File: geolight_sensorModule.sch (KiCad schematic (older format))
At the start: 19 parts, among them IC1 ATTINY841-SSU, P1 5V, P2 ICSP, P3 IN, P4 OUT, P5 AUX_SENSOR, P6 UART, U1 TCRT5000/L, Y1 16Mhz

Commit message: re-arranged PCB, routing done (all except ground plane)
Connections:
- net RESET: now also IC1.4 ((PCINT11/dW/~RESET~/ADC9)PB3), R4.2
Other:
- moved on the sheet: R4
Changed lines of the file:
@@
 L +5V #PWR01
 U 1 1 57C9E241
-P 3050 2300
-F 0 "#PWR01" H 3050 2150 50  0001 C CNN
-F 1 "+5V" H 3050 2440 50  0000 C CNN
-F 2 "" H 3050 2300 50  0000 C CNN
-F 3 "" H 3050 2300 50  0000 C CNN
-	1    3050 2300
+P 2850 2300
+F 0 "#PWR01" H 2850 2150 50  0001 C CNN
+F 1 "+5V" H 2850 2440 50  0000 C CNN
+F 2 "" H 2850 2300 50  0000 C CNN
+F 3 "" H 2850 2300 50  0000 C CNN
+	1    2850 2300
 	1    0    0    -1
 $EndComp
@@
 U 1 1 57CBB75B
 P 2950 4400
-F 0 "Y1" V 3150 4450 60  0000 C CNN
+F 0 "Y1" V 3100 4600 60  0000 C CNN
 F 1 "16Mhz" V 2750 4450 60  0000 C CNN
 F 2 "Crystals:Resonator_3.2x1.3mm" H 2970 4360 60  0001 C CNN
@@
 L R_Small R4
 U 1 1 57CC33DC
-P 3050 3800
-F 0 "R4" H 2900 3950 50  0000 L CNN
-F 1 "10k" V 2950 3750 50  0000 L CNN
-F 2 "Resistors_SMD:R_0603" H 3050 3800 50  0001 C CNN
-F 3 "" H 3050 3800 50  0000 C CNN
-	1    3050 3800
+P 2850 3800
+F 0 "R4" H 2700 3950 50  0000 L CNN
+F 1 "10k" V 2750 3750 50  0000 L CNN
+F 2 "Resistors_SMD:R_0603" H 2850 3800 50  0001 C CNN
+F 3 "" H 2850 3800 50  0000 C CNN
+	1    2850 3800
 	1    0    0    -1
 $EndComp
@@
 	5200 2300 5200 2350
 Wire Wire Line
-	5550 2350 5900 2350
+	5550 2350 5700 2350
+Wire Wire Line
+	5700 2350 5900 2350
 Wire Wire Line
 	5250 3600 5450 3600
@@
 	4500 2300 4500 2400
 Wire Wire Line
-	4300 2400 4700 2400
+	4300 2400 4500 2400
+Wire Wire Line
+	4500 2400 4700 2400
 Connection ~ 4500 2800
 Wire Wire Line
 	4500 2900 4500 2800
 Wire Wire Line
-	4300 2800 4700 2800
+	4300 2800 4500 2800
+Wire Wire Line
+	4500 2800 4700 2800
 Wire Wire Line
 	4700 2400 4700 2500
 Wire Wire Line
 	4700 2800 4700 2700
-Connection ~ 3050 3400
-Wire Wire Line
-	3050 2300 3050 3700
-Wire Wire Line
-	3050 4200 3050 3900
-Wire Wire Line
-	3150 4200 3050 4200
+Connection ~ 2850 3400
+Wire Wire Line
+	2850 2300 2850 3400
+Wire Wire Line
+	2850 3400 2850 3700
+Wire Wire Line
+	2850 4200 2850 3900
+Wire Wire Line
+	3150 4200 2850 4200
 Wire Wire Line
 	2150 2550 2150 2300
@@
 	5250 3400 5700 3400
 Wire Wire Line
-	3050 3400 3150 3400
+	2850 3400 3150 3400
 Wire Wire Line
 	3100 4600 3100 4750
@@
 	2750 4400 2500 4400
 Wire Wire Line
-	2500 4400 2500 4850
+	2500 4400 2500 4750
+Wire Wire Line
+	2500 4750 2500 4850
 Wire Wire Line
 	5900 2650 5850 2650
@@
 	6850 4100 5250 4100
 Wire Wire Line
-	5850 2900 6750 2900
+	5850 2900 6300 2900
+Wire Wire Line
+	6300 2900 6750 2900
 Connection ~ 6300 2900
 Wire Wire Line
@@
 Connection ~ 8050 3900
 Wire Wire Line
-	7550 3900 8550 3900
-Wire Wire Line
-	8200 4000 9600 4000
+	7550 3900 8050 3900
+Wire Wire Line
+	8050 3900 8550 3900
+Wire Wire Line
+	8200 4000 8350 4000
+Wire Wire Line
+	8350 4000 9600 4000
 Wire Wire Line
 	7550 4000 8050 4000
@@
 Wire Wire Line
 	9500 2650 9500 2900
+Text Label 2850 4200 0    60   ~ 0
+RESET
 $EndSCHEMATC

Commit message: finished v0.99 (no top copper pour)
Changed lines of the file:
@@
 	5200 2300 5200 2350
 Wire Wire Line
-	5550 2350 5700 2350
-Wire Wire Line
-	5700 2350 5900 2350
+	5550 2350 5900 2350
 Wire Wire Line
 	5250 3600 5450 3600
@@
 	4500 2300 4500 2400
 Wire Wire Line
-	4300 2400 4500 2400
-Wire Wire Line
-	4500 2400 4700 2400
+	4300 2400 4700 2400
 Connection ~ 4500 2800
 Wire Wire Line
 	4500 2900 4500 2800
 Wire Wire Line
-	4300 2800 4500 2800
-Wire Wire Line
-	4500 2800 4700 2800
+	4300 2800 4700 2800
 Wire Wire Line
 	4700 2400 4700 2500
@@
 Connection ~ 2850 3400
 Wire Wire Line
-	2850 2300 2850 3400
-Wire Wire Line
-	2850 3400 2850 3700
+	2850 2300 2850 3700
 Wire Wire Line
 	2850 4200 2850 3900
@@
 	2750 4400 2500 4400
 Wire Wire Line
-	2500 4400 2500 4750
-Wire Wire Line
-	2500 4750 2500 4850
+	2500 4400 2500 4850
 Wire Wire Line
 	5900 2650 5850 2650
@@
 	6850 4100 5250 4100
 Wire Wire Line
-	5850 2900 6300 2900
-Wire Wire Line
-	6300 2900 6750 2900
+	5850 2900 6750 2900
 Connection ~ 6300 2900
 Wire Wire Line
@@
 Connection ~ 8050 3900
 Wire Wire Line
-	7550 3900 8050 3900
+	7550 3900 8550 3900
 Wire Wire Line
-	8050 3900 8550 3900
-Wire Wire Line
-	8200 4000 8350 4000
-Wire Wire Line
-	8350 4000 9600 4000
+	8200 4000 9600 4000
 Wire Wire Line
 	7550 4000 8050 4000

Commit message: minor modifications? pre-rev2
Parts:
- C1: value 10-220uF -> OPEN
- IC1: MFR (none) -> Atmel; MPN (none) -> ATTINY841-SSU; SPN (none) -> ATTINY841-SSU-ND; SPR (none) -> Digikey
- JP1: value I2C/SS -> OPEN
- JP2: value MISO EN -> OPEN
- P1: value 5V -> OPEN
- P2: value ICSP -> OPEN
- P3: value IN -> Male Pin Header, Angled (90*)
- P4: value OUT -> Male Pin Header, Angled (90*)
- P5: value AUX_SENSOR -> OPEN
- P6: value UART -> OPEN
- R1, R5: value 220? -> 220
- U1: MFR (none) -> Vishay; MPN (none) -> TCRT5000L; SPN (none) -> 751-1034-5-ND; SPR (none) -> digikey
- Y1: MFR (none) -> Murata; MPN (none) -> CSTCE16M0V53-R0; SPN (none) -> 490-1198-1-ND; SPR (none) -> Digikey

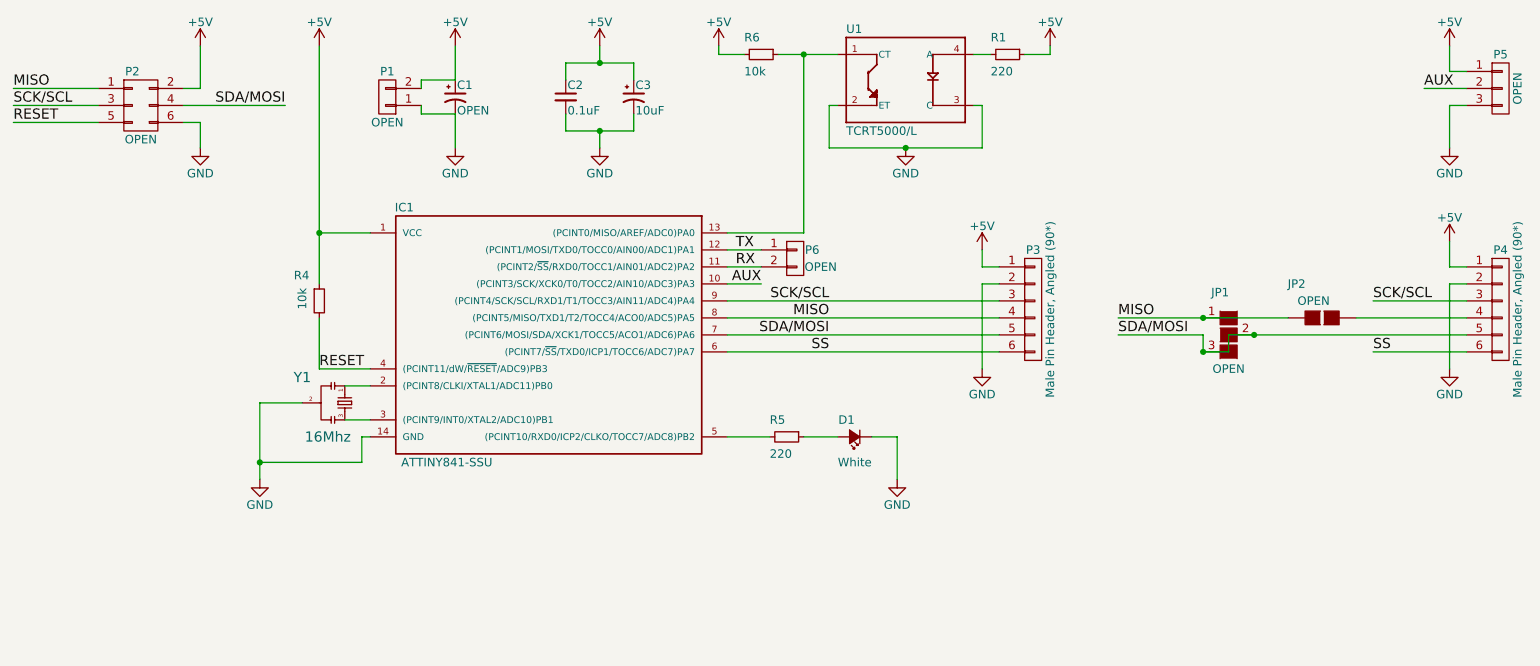
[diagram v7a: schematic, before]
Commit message: removed empty path cap, changed all 0603 to 0603_handsolder, fixed I2C wiring order, left SPI channels but most likely unused.
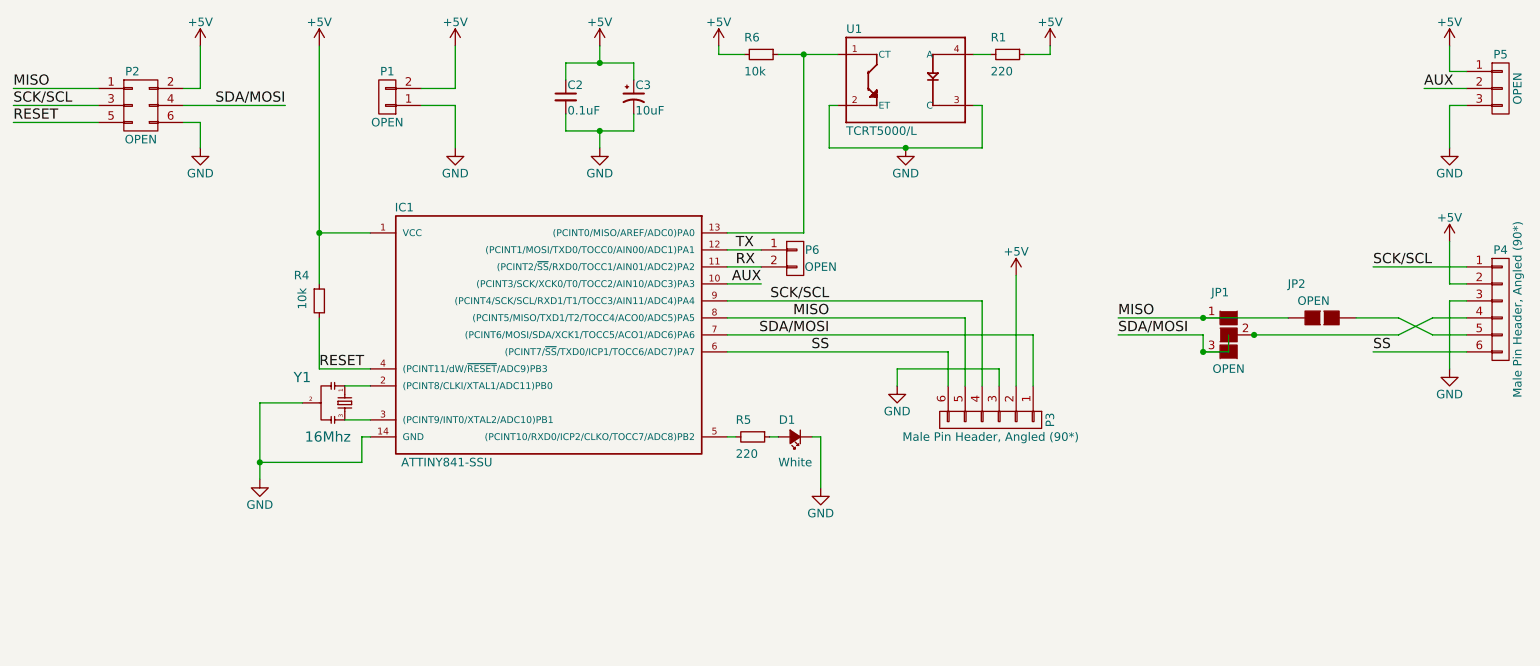
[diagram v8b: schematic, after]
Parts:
- removed C1: OPEN, Capacitors_ThroughHole:C_Radial_D5_L6_P2.5, symbol CP1_Small
- C2: footprint Capacitors_SMD:C_0603 -> Capacitors_SMD:C_0603_HandSoldering
- D1: footprint LEDs:LED-3MM -> LEDs:LED-8MM
- R1, R4, R5, R6: footprint Resistors_SMD:R_0603 -> Resistors_SMD:R_0603_HandSoldering
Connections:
- net +5V: now also P3.2 (P2), P4.2 (P2); no longer P3.1 (P1), P4.1 (P1)
- net GND: now also P3.3 (P3), P4.3 (P3); no longer P3.2 (P2), P4.2 (P2)
- net MISO: now also P3.5 (P5); no longer P3.4 (P4)
- net SCK/SCL: now also P3.4 (P4), P4.1 (P1); no longer P3.3 (P3), P4.3 (P3)
- net SDA/MOSI: now also P3.1 (P1); no longer JP1.2 (G2), P3.5 (P5), P4.5 (P5)
- net at P4.4 (P4): now also JP1.2 (G2); no longer JP2.1 (G1)
- new net: JP2.1 (G1), P4.5 (P5)
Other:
- moved on the sheet: D1, P3, R5
